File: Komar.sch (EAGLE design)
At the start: 112 parts, among them CON1 USB-VERTICAL, CON10 PINHEAD_1X01-2, CON11 PINHEAD_1X01-2, CON12 PINHEAD_1X01-2, CON13 PINHEAD_1X01-2, CON14 PINHEAD_1X01-2, CON15 PINHEAD_1X01-2, CON2 PINHEAD_1X01-2, CON3 CON-4P-TABS-STRAIGHT, CON4 CON-4P-TABS-STRAIGHT, CON5 CON-4P-TABS-STRAIGHT, CON6 CON-4P-TABS-STRAIGHT, CON7 CON-4P-TABS-STRAIGHT, CON8 PINHEAD_1X04-2, CON9 PINHEAD_1X01-2, IC1 TPD3S014DBVR-SOT23-6, IC2 TPD3S014DBVR-SOT23-6, IC3 ATA6561-GBQW-N-HVSON8, IC4 ATA6561-GBQW-N-HVSON8, IC5 MCP9700AT-E/TTVAO-SOT23, IC6 11LC040T-E/TT, Q1 FDMS86368-F085, Q10 FDMS86368-F085, Q11 FDMS86368-F085, Q12 FDMS86368-F085, Q2 FDMS86368-F085, Q3 FDMS86368-F085, Q4 FDMS86368-F085, Q5 FDMS86368-F085, Q6 FDMS86368-F085, Q7 FDMS86368-F085, Q8 FDMS86368-F085, Q9 FDMS86368-F085

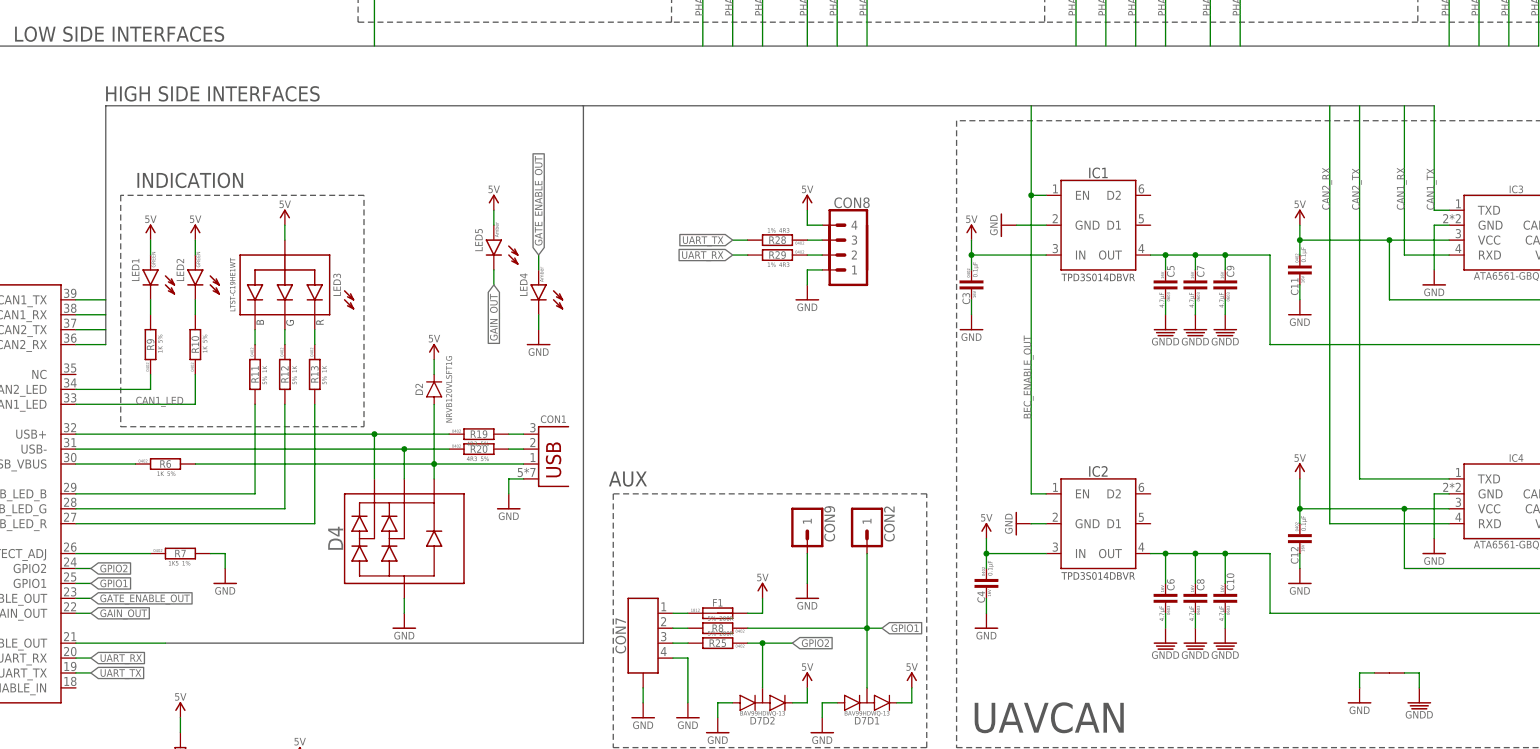
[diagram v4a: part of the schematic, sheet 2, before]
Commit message: changed usb back to through-hole
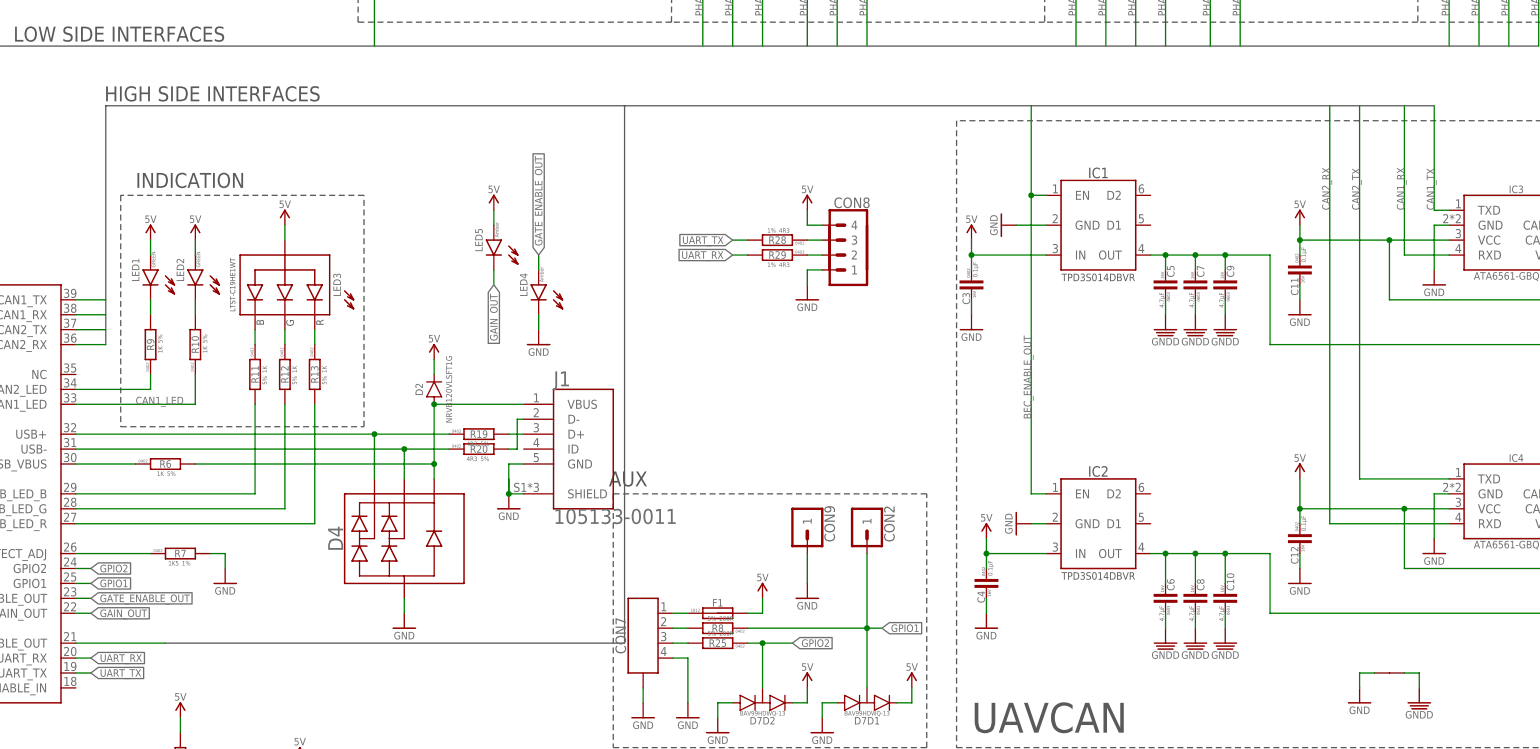
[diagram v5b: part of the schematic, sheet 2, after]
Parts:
- removed CON1: USB-VERTICAL, Connectors:USB-VERTICAL
- added J1: 105133-0011, 105133-0011:105133-0011
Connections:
- removed net N$52: CON1.D+, R19.2
- removed net N$54: CON1.D-, R20.2
- new net N$1: J1.D+, R19.2
- new net N$2: J1.D-, R20.2
- net GND: now also J1.GND, J1.SHIELD; no longer CON1.GND
- net USB_VBUS: now also J1.VBUS; no longer CON1.VBUS
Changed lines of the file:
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@@
 <?xml version="1.0" encoding="utf-8"?>
 <!DOCTYPE eagle SYSTEM "eagle.dtd">
-<eagle version="9.6.1">
+<eagle version="9.6.2">
 <drawing>
 <settings>
@@
 <setting verticaltext="up"/>
 </settings>
-<grid distance="0.1" unitdist="inch" unit="inch" style="lines" multiple="1" display="no" altdistance="0.01" altunitdist="inch" altunit="inch"/>
+<grid distance="1" unitdist="mm" unit="mm" style="lines" multiple="1" display="no" altdistance="0.1" altunitdist="mm" altunit="mm"/>
 <layers>
 <layer number="1" name="Top" color="4" fill="1" visible="no" active="no"/>
@@
 <part name="+P7" library="supply_symbols" library_urn="urn:adsk.eagle:library:5017758" deviceset="VDC" device=""/>
 <part name="+P8" library="supply_symbols" library_urn="urn:adsk.eagle:library:5017758" deviceset="VDC" device=""/>
-<part name="CON1" library="Connectors" library_urn="urn:adsk.eagle:library:3750510" deviceset="USB" device="-VERTICAL" package3d_urn="urn:adsk.eagle:package:4410721/4">
-<attribute name="AEC-Q" value="---"/>
-<attribute name="OPERATING_TEMP" value="-35°C ~ 85°C"/>
-</part>
 <part name="D4" library="TVS_diodes" library_urn="urn:adsk.eagle:library:3333632" deviceset="DRTR5V0U2SR-7" device="" package3d_urn="urn:adsk.eagle:package:3333649/3"/>
 <part name="+P19" library="supply_symbols" library_urn="urn:adsk.eagle:library:5017758" deviceset="5V" device=""/>
@@
 <variant name="BASIC" populate="no"/>
 </part>
+<part name="J1" library="105133-0011" deviceset="105133-0011" device=""/>
 </parts>
 <sheets>
@@
 <attribute name="VALUE" x="43.18" y="227.076" size="1.27" layer="96" font="vector" ratio="15" align="center"/>
 </instance>
-<instance part="CON1" gate="G$1" x="167.64" y="76.2" smashed="yes">
-<attribute name="OPERATING_TEMP" x="167.64" y="76.2" size="1.778" layer="96" font="vector" ratio="15" align="center" display="off"/>
-<attribute name="AEC-Q" x="167.64" y="76.2" size="1.27" layer="96" font="vector" ratio="15" align="center" display="off"/>
-<attribute name="NAME" x="170.18" y="86.36" size="1.27" layer="95" font="vector" ratio="15" align="center"/>
-</instance>
 <instance part="D4" gate="G$1" x="134.62" y="58.42" smashed="yes">
 <attribute name="NAME" x="133.096" y="66.04" size="2.54" layer="95" font="vector" ratio="15" rot="R90" align="center"/>
@@
 <attribute name="NAME" x="207.01" y="10.16" size="1.778" layer="95" font="vector" ratio="15" rot="R90" align="center"/>
 </instance>
+<instance part="J1" gate="G$1" x="175.26" y="81.28" smashed="yes">
+<attribute name="NAME" x="170.17251875" y="91.9637" size="2.541159375" layer="95"/>
+<attribute name="VALUE" x="170.16298125" y="68.5451" size="2.540890625" layer="96"/>
+</instance>
 </instances>
 <busses>
@@
 <bus name="BEC_ENABLE_OUT,CAN1_RX,CAN1_TX,CAN2_RX,CAN2_TX">
 <segment>
-<wire x1="320.04" y1="139.7" x2="175.26" y2="139.7" width="0.762" layer="92"/>
+<wire x1="320.04" y1="139.7" x2="182.26" y2="139.7" width="0.762" layer="92"/>
 <wire x1="93.98" y1="99.06" x2="93.98" y2="139.7" width="0.762" layer="92"/>
-<wire x1="93.98" y1="139.7" x2="175.26" y2="139.7" width="0.762" layer="92"/>
-<wire x1="175.26" y1="139.7" x2="175.26" y2="48.26" width="0.762" layer="92"/>
-<wire x1="175.26" y1="48.26" x2="104.14" y2="48.26" width="0.762" layer="92"/>
+<wire x1="93.98" y1="139.7" x2="182.26" y2="139.7" width="0.762" layer="92"/>
+<wire x1="182.26" y1="139.7" x2="182.26" y2="48.26" width="0.762" layer="92"/>
+<wire x1="182.26" y1="48.26" x2="104.14" y2="48.26" width="0.762" layer="92"/>
 </segment>
 </bus>
@@
 </segment>
 <segment>
-<wire x1="162.56" y1="76.2" x2="165.1" y2="76.2" width="0.1524" layer="91"/>
 <pinref part="GND11" gate="1" pin="GND"/>
 <wire x1="162.56" y1="76.2" x2="162.56" y2="73.66" width="0.1524" layer="91"/>
-<pinref part="CON1" gate="G$1" pin="GND"/>
+<pinref part="J1" gate="G$1" pin="GND"/>
+<wire x1="165.1" y1="78.74" x2="162.56" y2="78.74" width="0.1524" layer="91"/>
+<wire x1="162.56" y1="78.74" x2="162.56" y2="73.66" width="0.1524" layer="91"/>
+<junction x="162.56" y="73.66"/>
+<pinref part="J1" gate="G$1" pin="SHIELD"/>
+<wire x1="165.1" y1="73.66" x2="162.56" y2="73.66" width="0.1524" layer="91"/>
 </segment>
 <segment>
@@
 <net name="USB_VBUS" class="0">
 <segment>
-<wire x1="165.1" y1="78.74" x2="149.86" y2="78.74" width="0.1524" layer="91"/>
 <junction x="149.86" y="78.74"/>
 <pinref part="D2" gate="G$1" pin="A"/>
 <wire x1="149.86" y1="78.74" x2="149.86" y2="88.9" width="0.1524" layer="91"/>
-<pinref part="CON1" gate="G$1" pin="VBUS"/>
 <pinref part="D4" gate="G$1" pin="A"/>
 <wire x1="149.86" y1="76.2" x2="149.86" y2="78.74" width="0.1524" layer="91"/>
 <pinref part="R6" gate="G$1" pin="2"/>
 <wire x1="109.22" y1="78.74" x2="149.86" y2="78.74" width="0.1524" layer="91"/>
-</segment>
-</net>
-<net name="N$52" class="0">
-<segment>
-<pinref part="R19" gate="G$1" pin="2"/>
-<wire x1="162.56" y1="83.82" x2="165.1" y2="83.82" width="0.1524" layer="91"/>
-<pinref part="CON1" gate="G$1" pin="D+"/>
-</segment>
-</net>
-<net name="N$54" class="0">
-<segment>
-<pinref part="R20" gate="G$1" pin="2"/>
-<wire x1="162.56" y1="81.28" x2="165.1" y2="81.28" width="0.1524" layer="91"/>
-<pinref part="CON1" gate="G$1" pin="D-"/>
+<pinref part="J1" gate="G$1" pin="VBUS"/>
+<wire x1="165.1" y1="88.9" x2="149.86" y2="88.9" width="0.1524" layer="91"/>
+<junction x="149.86" y="88.9"/>
 </segment>
 </net>
@@
 </segment>
 </net>
+<net name="N$1" class="0">
+<segment>
+<pinref part="R19" gate="G$1" pin="2"/>
+<pinref part="J1" gate="G$1" pin="D+"/>
+<wire x1="162.56" y1="83.82" x2="165.1" y2="83.82" width="0.1524" layer="91"/>
+</segment>
+</net>
+<net name="N$2" class="0">
+<segment>
+<pinref part="J1" gate="G$1" pin="D-"/>
+<wire x1="165.1" y1="86.36" x2="164" y2="86.36" width="0.1524" layer="91"/>
+<wire x1="164" y1="86.36" x2="164" y2="81.28" width="0.1524" layer="91"/>
+<pinref part="R20" gate="G$1" pin="2"/>
+<wire x1="164" y1="81.28" x2="162.56" y2="81.28" width="0.1524" layer="91"/>
+</segment>
+</net>

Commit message: minor changes to fixes #26
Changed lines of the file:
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@@
 <setting verticaltext="up"/>
 </settings>
-<grid distance="1" unitdist="mm" unit="mm" style="lines" multiple="1" display="no" altdistance="0.1" altunitdist="mm" altunit="mm"/>
+<grid distance="0.1" unitdist="inch" unit="inch" style="lines" multiple="1" display="no" altdistance="0.01" altunitdist="inch" altunit="inch"/>
 <layers>
 <layer number="1" name="Top" color="4" fill="1" visible="no" active="no"/>
@@
 <text x="142.24" y="160.02" size="2.54" layer="97">Place close to power mosfets</text>
 <text x="182.88" y="76.2" size="2.54" layer="97" font="vector" ratio="15" align="center">AUX</text>
-<wire x1="180.34" y1="73.66" x2="180.34" y2="30.48" width="0.1524" layer="97" style="shortdash"/>
+<wire x1="180.34" y1="71.12" x2="180.34" y2="30.48" width="0.1524" layer="97" style="shortdash"/>
 <wire x1="180.34" y1="30.48" x2="233.68" y2="30.48" width="0.1524" layer="97" style="shortdash"/>
-<wire x1="233.68" y1="30.48" x2="233.68" y2="73.66" width="0.1524" layer="97" style="shortdash"/>
-<wire x1="233.68" y1="73.66" x2="180.34" y2="73.66" width="0.1524" layer="97" style="shortdash"/>
+<wire x1="233.68" y1="30.48" x2="233.68" y2="71.12" width="0.1524" layer="97" style="shortdash"/>
+<wire x1="233.68" y1="71.12" x2="180.34" y2="71.12" width="0.1524" layer="97" style="shortdash"/>
 <text x="5.08" y="269.24" size="2.54" layer="97" font="vector" ratio="15" align="center-left">Power should be connected with multi-strand 12AWG wire in silicone insulation</text>
 <text x="68.58" y="276.86" size="2.54" layer="97" font="vector" ratio="15" align="center">PCB hole diameters for wires are based on the chart from PCBLibraries.com
